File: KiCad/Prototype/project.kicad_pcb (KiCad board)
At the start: 2 copper layers, 68.6 x 53.3 mm, 40 parts, among them J3 Barrel_Jack, Q1 PMOS, SW1 RESET, U1 LP2985-3.3, U2 LMV358, U3 NCP1117-1.5, U4 ATMEGA32U4-AU, X1 USB_OTG, Y1 16 Mhz

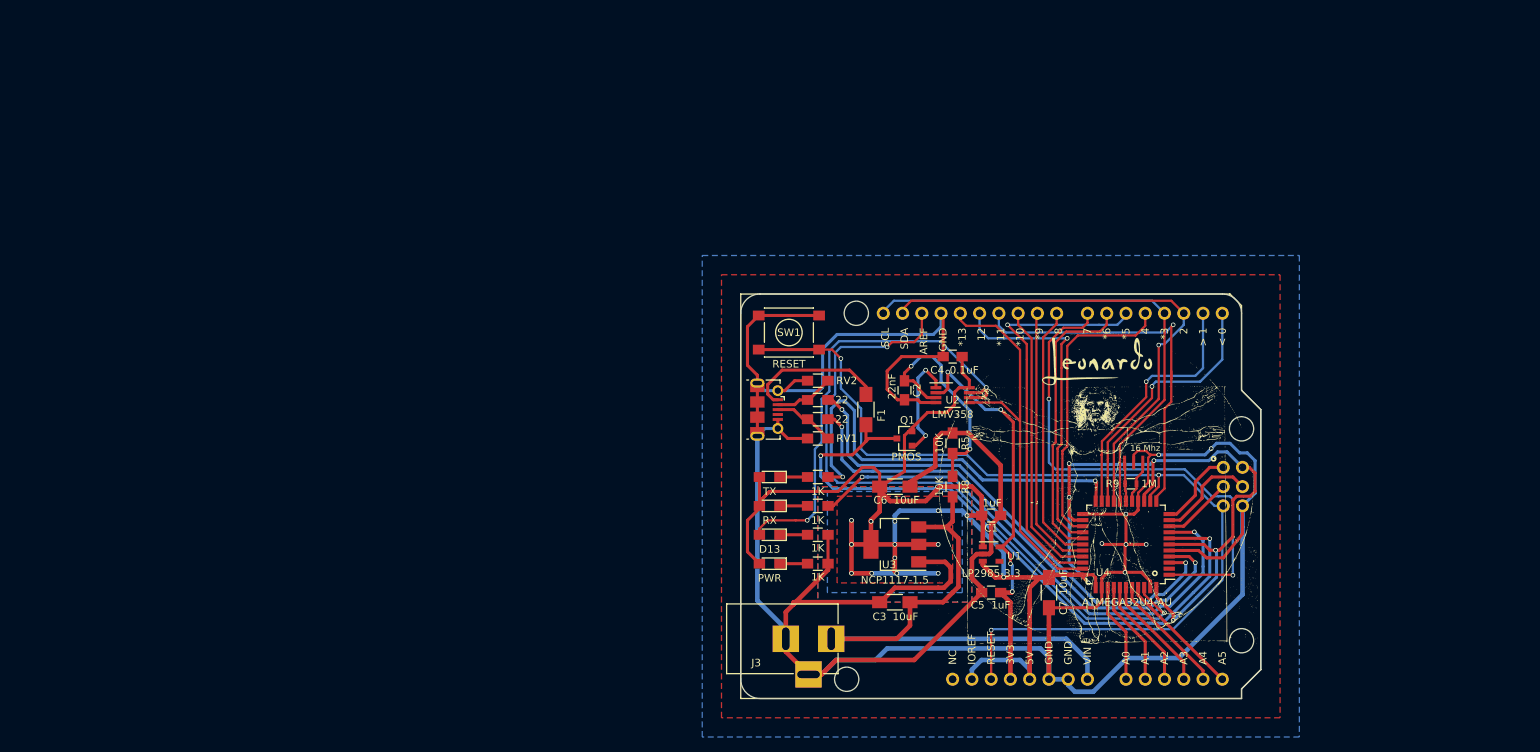
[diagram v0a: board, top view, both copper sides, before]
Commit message: more work on schematic, started layout
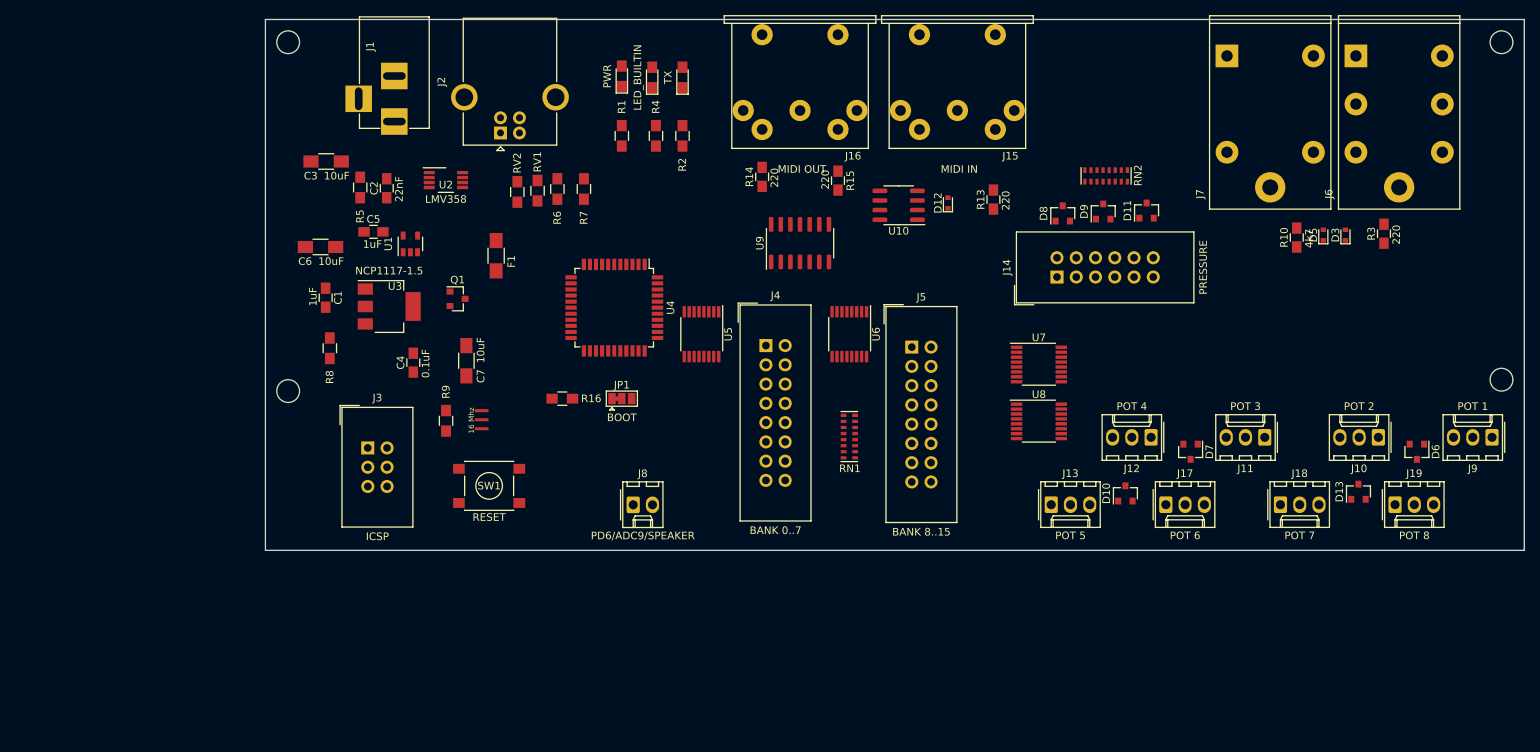
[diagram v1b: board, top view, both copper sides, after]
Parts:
- removed G***: LOGO, footprints:Leo_Front
- removed G***: LOGO, footprints:Leo_back
- removed G*** (x2): LOGO, footprints:graphic_SDA
- removed REF***: KiCad-Logo2_8mm_SilkScreen, Symbols:KiCad-Logo2_8mm_SilkScreen
- removed REF***: OSHW-Logo_5.7x6mm_SilkScreen, Symbols:OSHW-Logo_5.7x6mm_SilkScreen
- removed VAL: MadeInOregonRev25, footprints:MadeInOregonRev25
- removed X1: USB_OTG, footprints:USB_Micro-B_Molex-105017-0001
- removed XA1: Arduino_Leonardo_Shield, footprints:Arduino_Leonardo_Shield
- added D10: BAV70, footprints:SOT-23, F.Cu at (157.4, 102.5)
- added D11: BAV70, footprints:SOT-23, F.Cu at (160.2, 65.2)
- added D12: 1N914WT, footprints:D_SOD-523, F.Cu at (134.0, 64.2)
- added D13: BAV70, footprints:SOT-23, F.Cu at (188.1, 102.3)
- added D5: 1N914WT, footprints:D_SOD-523, F.Cu at (183.5, 68.4)
- added D6: BAV70, footprints:SOT-23, F.Cu at (195.8, 97.0)
- added D7: BAV70, footprints:SOT-23, F.Cu at (166.0, 97.0)
- added D8: BAV70, footprints:SOT-23, F.Cu at (149.1, 65.6)
- added D9: BAV70, footprints:SOT-23, F.Cu at (154.5, 65.3)
- added J1: Barrel_Jack, footprints:BARREL_JACK, F.Cu at (61.0, 53.5)
- added J10: POT 2, footprints:Molex_KK-254_AE-6410-03A_1x03_P2.54mm_Vertical, F.Cu at (190.8, 95.1)
- added J11: POT 3, footprints:Molex_KK-254_AE-6410-03A_1x03_P2.54mm_Vertical, F.Cu at (175.8, 95.1)
- added J12: POT 4, footprints:Molex_KK-254_AE-6410-03A_1x03_P2.54mm_Vertical, F.Cu at (160.8, 95.1)
- added J13: POT 5, footprints:Molex_KK-254_AE-6410-03A_1x03_P2.54mm_Vertical, F.Cu at (147.6, 104.0)
- added J14: PRESSURE, footprints:IDC-Header_2x06_P2.54mm_Vertical, F.Cu at (148.4, 74.0)
- added J15: MIDI IN, footprints:DIN_5_180Deg_PSG03463, F.Cu at (135.2, 52.0)
- added J16: MIDI OUT, footprints:DIN_5_180Deg_PSG03463, F.Cu at (114.5, 52.0)
- added J17: POT 6, footprints:Molex_KK-254_AE-6410-03A_1x03_P2.54mm_Vertical, F.Cu at (162.7, 104.0)
- added J18: POT 7, footprints:Molex_KK-254_AE-6410-03A_1x03_P2.54mm_Vertical, F.Cu at (177.8, 104.0)
- added J19: POT 8, footprints:Molex_KK-254_AE-6410-03A_1x03_P2.54mm_Vertical, F.Cu at (193.0, 104.0)
- added J2: USB_B, footprints:USB_B_OST_USB-B1HSxx_Horizontal, F.Cu at (75.0, 55.0)
- added J4: BANK 0..7, footprints:IDC-Header_2x08_P2.54mm_Vertical, F.Cu at (110.0, 83.0)
- added J5: BANK 8..15, footprints:IDC-Header_2x08_P2.54mm_Vertical, F.Cu at (129.2, 83.2)
- added J6: EXPRESSION, footprints:Jack_6.35mm_Amphenol_ACJS-MHDR, F.Cu at (193.5, 57.5)
- added J7: SUSTAIN, footprints:Jack_6.35mm_Amphenol_ACJM-MHDR, F.Cu at (176.5, 57.5)
- added J8: PD6/ADC9/SPEAKER, footprints:Molex_KK-254_AE-6410-02A_1x02_P2.54mm_Vertical, F.Cu at (92.5, 104.0)
- added J9: POT 1, footprints:Molex_KK-254_AE-6410-03A_1x03_P2.54mm_Vertical, F.Cu at (205.7, 95.1)
- added JP1: BOOT, footprints:SolderJumper-3_P1.3mm_Bridged12_Pad1.0x1.5mm, F.Cu at (91.0, 90.0)
- added R10: 4k7, footprints:C_0805_HandSoldering, F.Cu at (180.0, 68.8)
- added R13: 220, footprints:C_0805_HandSoldering, F.Cu at (140.0, 63.8)
- added R14: 220, footprints:C_0805_HandSoldering, F.Cu at (109.5, 60.8)
- added R15: 220, footprints:C_0805_HandSoldering, F.Cu at (119.5, 61.2)
- added R16: 1K, footprints:R_0805_HandSoldering, F.Cu at (83.2, 90.0)
- added RN1: 4k7, footprints:R_Cat16-8, F.Cu at (121.0, 95.0)
- added RN2: 10k/4k7, footprints:R_Cat16-8, F.Cu at (154.9, 60.6)
- added U10: HCPL-0600, footprints:SOIC-8_3.9x4.9mm_P1.27mm, F.Cu at (127.5, 64.5)
- added U5: 74LS138, footprints:TSSOP-16_4.4x5mm_P0.65mm, F.Cu at (101.5, 81.5)
- added U6: 74LS138, footprints:TSSOP-16_4.4x5mm_P0.65mm, F.Cu at (121.0, 81.5)
- added U7: 74LS238, footprints:TSSOP-16_4.4x5mm_P0.65mm, F.Cu at (146.0, 85.5)
- added U8: 74LS238, footprints:TSSOP-16_4.4x5mm_P0.65mm, F.Cu at (146.0, 93.0)
- added U9: 74HC04, footprints:SOIC-14_3.9x8.7mm_P1.27mm, F.Cu at (114.5, 69.5)
- C1, C2, C4, C5: footprint Capacitors_SMD:C_0805_HandSoldering -> footprints:C_0805_HandSoldering
- C3, C6: footprint Capacitors_SMD:C_1206_HandSoldering -> footprints:C_1206_HandSoldering
- D1, D2: footprint LEDs:LED_0805_HandSoldering -> footprints:LED_0805_HandSoldering
- D3: value RX -> 1N914WT; footprint LEDs:LED_0805_HandSoldering -> footprints:D_SOD-523
- D4: value D13 -> LED_BUILTIN; footprint LEDs:LED_0805_HandSoldering -> footprints:LED_0805_HandSoldering
- F1: footprint Resistors_SMD:R_1206_HandSoldering -> footprints:R_1206_HandSoldering
- J3: value Barrel_Jack -> ICSP; footprint Connectors:BARREL_JACK -> footprints:IDC-Header_2x03_P2.54mm_Vertical
- Q1: footprint TO_SOT_Packages_SMD:SOT-23 -> footprints:SOT-23
- R1, R2, R4, R5, R6, R7, R8, RV1, RV2: footprint Resistors_SMD:R_0805_HandSoldering -> footprints:R_0805_HandSoldering
- R3: value 1K -> 220; footprint Resistors_SMD:R_0805_HandSoldering -> footprints:C_0805_HandSoldering
- R9: footprint Resistors_SMD:R_0603 -> footprints:R_0805_HandSoldering
- SW1: footprint Buttons_Switches_SMD:SW_SPST_PTS645 -> footprints:SW_SPST_PTS645
- U1: footprint TO_SOT_Packages_SMD:SOT-23-5 -> footprints:SOT-23-5
- U2: footprint Housings_SSOP:VSSOP-8_3.0x3.0mm_Pitch0.65mm -> footprints:VSSOP-8_3.0x3.0mm_Pitch0.65mm
- U3: footprint TO_SOT_Packages_SMD:SOT-223-3_TabPin2 -> footprints:SOT-223-3_TabPin2
- moved C3 94.9 mm to (52.0, 58.7)
- moved C5 94.3 mm to (58.2, 68.0)
- moved C1 92.3 mm to (51.9, 76.7), turned to 90 degrees
- moved R9 90.7 mm to (67.8, 92.9), turned to 270 degrees
- moved U1 86.8 mm to (63.1, 69.6), turned to 90 degrees
- moved Y1 86.2 mm to (72.5, 92.8), turned to 90 degrees
- moved R5 85.1 mm to (56.5, 62.1), turned to 90 degrees
- moved R8 84.1 mm to (52.5, 83.3), turned to 90 degrees
- moved D3 83.9 mm to (186.4, 68.4), turned to 90 degrees
- moved R3 82.8 mm to (191.5, 68.2), turned to 270 degrees
- moved C7 82.7 mm to (70.5, 85.0)
- moved C6 82.1 mm to (51.3, 70.0), turned to 180 degrees
- moved U4 74.4 mm to (90.0, 78.0), turned to 270 degrees
- moved U3 73.7 mm to (60.3, 77.9), turned to 0 degrees
- moved C2 73.3 mm to (60.0, 62.2)
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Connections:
- C3 pad 1: /VIN -> +12V
- D3 pad 1: Net-(D3-Pad1) -> /ADC10
- D3 pad 2: +5V -> Net-(D3-Pad2)
- J3 pad 1: /VIN -> /PB3
- J3 pad 2: GND -> +5V
- J3 pad 3: GND -> /PB1
- R3 pad 1: /RXLED -> Net-(J6-PadR)
- R3 pad 2: Net-(D3-Pad1) -> /AMUX1
- R8 pad 2: /VIN -> +12V
- U3 pad 3: /VIN -> +12V
- U4 pad 1: /D7 -> /PE6
- U4 pad 10: /MOSI -> /PB2
- U4 pad 11: /MISO -> /PB3
- U4 pad 12: /D11 -> /PB7
- U4 pad 20: /D0 -> /RXD
- U4 pad 21: /D1 -> /TXD
- U4 pad 25: /D4 -> /PD4
- U4 pad 26: /D12 -> /ADC9
- U4 pad 27: /D6 -> /ADC10
- U4 pad 28: /D8 -> /PB4
- U4 pad 29: /D9 -> /PB5
- U4 pad 30: /D10 -> /PB6
- U4 pad 33: +5V -> /~HWB
- U4 pad 36: /A0 -> /PF7
- U4 pad 37: /A1 -> /PF6
- U4 pad 38: /A2 -> /PF5
- U4 pad 39: /A3 -> /PF4
- U4 pad 40: /A4 -> /PF1
- U4 pad 41: /A5 -> /PF0
- U4 pad 8: /RXLED -> /PB0
- U4 pad 9: /SCK -> /PB1
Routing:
- net GND: track 417.4 -> 0.00 mm, vias 7 -> 0
- net +5V: track 291.0 -> 0.00 mm, vias 20 -> 0
- net /~RESET: track 128.7 -> 0.00 mm, vias 3 -> 0
- net /AREF: track 88.9 -> 0.00 mm, vias 2 -> 0
- net VBUS: track 88.4 -> 0.00 mm, vias 2 -> 0
- net /VIN: track 75.4 -> 0.00 mm
- net /RXLED: track 70.2 -> 0.00 mm, vias 2 -> 0
- net /D+: track 68.2 -> 0.00 mm, vias 2 -> 0
- net /D7: track 68.0 -> 0.00 mm, vias 2 -> 0
- net /SDA: track 67.7 -> 0.00 mm, vias 1 -> 0
- net /D-: track 66.5 -> 0.00 mm, vias 2 -> 0
- net /SCL: track 65.8 -> 0.00 mm
- net Net-(D4-Pad2): track 60.9 -> 0.00 mm, vias 2 -> 0
- net /TXLED: track 57.6 -> 0.00 mm, vias 2 -> 0
- net /D5: track 53.7 -> 0.00 mm, vias 1 -> 0
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- removed copper zone on B.Cu, net +5V
- removed copper zone on F.Cu, net +5V
- removed copper zone on B.Cu, net GND
- removed copper zone on F.Cu, net GND
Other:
- board size 68.6 x 53.3 mm -> 166 x 70 mm
- board text removed: "*10"
- board text removed: "*11"
- board text removed: "*13"
- board text removed: "*3"
- board text removed: "*5"
- board text removed: "*6"
- board text removed: "*9"
- board text removed: "12"
- board text removed: "2"
- board text removed: "3V3"
- board text removed: "4"
- board text removed: "5V"
- board text removed: "7"
- board text removed: "8"
- board text removed: "< 0"
- board text removed: "> 1"
- board text removed: "@TheMakerBox"
- board text removed: "A0"
- board text removed: "A1"
- board text removed: "A2"
- board text removed: "A3"
- board text removed: "A4"
- board text removed: "A5"
- board text removed: "AREF"
- board text removed: "GND"
- board text removed: "IOREF"
- board text removed: "NC"
- board text removed: "RESET"
- board text removed: "Rev 0.0 Sep 2018"
- board text removed: "SCL"
- board text removed: "SDA"
- board text removed: "VIN"
- board text removed: "www.MakersBox.us"

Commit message: more routing
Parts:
- RN1, RN2: footprint footprints:R_Cat16-8 -> Package_SO:SOIC-16_3.9x9.9mm_P1.27mm
- U5, U6, U7, U8: footprint footprints:TSSOP-16_4.4x5mm_P0.65mm -> Package_SO:SOIC-16_3.9x9.9mm_P1.27mm
- moved U8 52.8 mm to (196.0, 76.0), turned to 270 degrees
- moved U7 36.3 mm to (181.0, 76.0), turned to 270 degrees
- moved RN1 24.8 mm to (144.5, 103.0), turned to 90 degrees
- moved U6 22.9 mm to (143.5, 85.5), turned to 180 degrees
- moved U5 17.3 mm to (104.5, 98.5), turned to 0 degrees
- moved C6 17.2 mm to (57.5, 86.0), turned to 270 degrees
- moved D10 8.16 mm to (165.5, 103.5)
- moved D13 7.57 mm to (195.6, 103.3)
- moved J13 7.57 mm to (155.1, 105.0)
- moved J17 7.57 mm to (170.2, 105.0)
- moved J18 7.57 mm to (185.3, 105.0)
- moved J19 7.57 mm to (200.5, 105.0)
- moved R16 7.23 mm to (85.0, 97.0), turned to 0 degrees
- moved J8 7.02 mm to (85.5, 103.5)
- moved J3 6.95 mm to (54.0, 102.5), turned to 90 degrees
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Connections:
- RN1 pad 1: /PB0 -> +5V
- RN1 pad 10: +5V -> /PB6
- RN1 pad 11: +5V -> /PB5
- RN1 pad 12: +5V -> /PB4
- RN1 pad 13: +5V -> /PB3
- RN1 pad 14: +5V -> /PB2
- RN1 pad 15: +5V -> /PB1
- RN1 pad 16: +5V -> /PB0
- RN1 pad 2: /PB1 -> +5V
- RN1 pad 3: /PB2 -> +5V
- RN1 pad 4: /PB3 -> +5V
- RN1 pad 5: /PB4 -> +5V
- RN1 pad 6: /PB5 -> +5V
- RN1 pad 7: /PB6 -> +5V
- RN1 pad 8: /PB7 -> +5V
- RN1 pad 9: +5V -> /PB7
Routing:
- net /PF4: track 0.00 -> 140.6 mm, vias 0 -> 4
- net /PF5: track 0.00 -> 139.7 mm, vias 0 -> 4
- net /PF6: track 0.00 -> 137.9 mm, vias 0 -> 4
- net /PF7: track 0.00 -> 132.7 mm, vias 0 -> 4
- net /PB0: track 0.00 -> 95.6 mm, vias 0 -> 1
- net /PB1: track 0.00 -> 92.1 mm, vias 0 -> 2
- net /PB2: track 0.00 -> 88.5 mm, vias 0 -> 2
- net /PB3: track 0.00 -> 84.2 mm, vias 0 -> 2
- net GND: track 0.00 -> 82.9 mm
- net /PB7: track 0.00 -> 78.7 mm, vias 0 -> 2
- net /PB4: track 0.00 -> 67.2 mm, vias 0 -> 2
- net /PB5: track 0.00 -> 67.0 mm, vias 0 -> 2
- net /PB6: track 0.00 -> 67.0 mm, vias 0 -> 2
- net /~RESET: track 0.00 -> 51.9 mm
- net /AMUX2: track 0.00 -> 38.2 mm
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
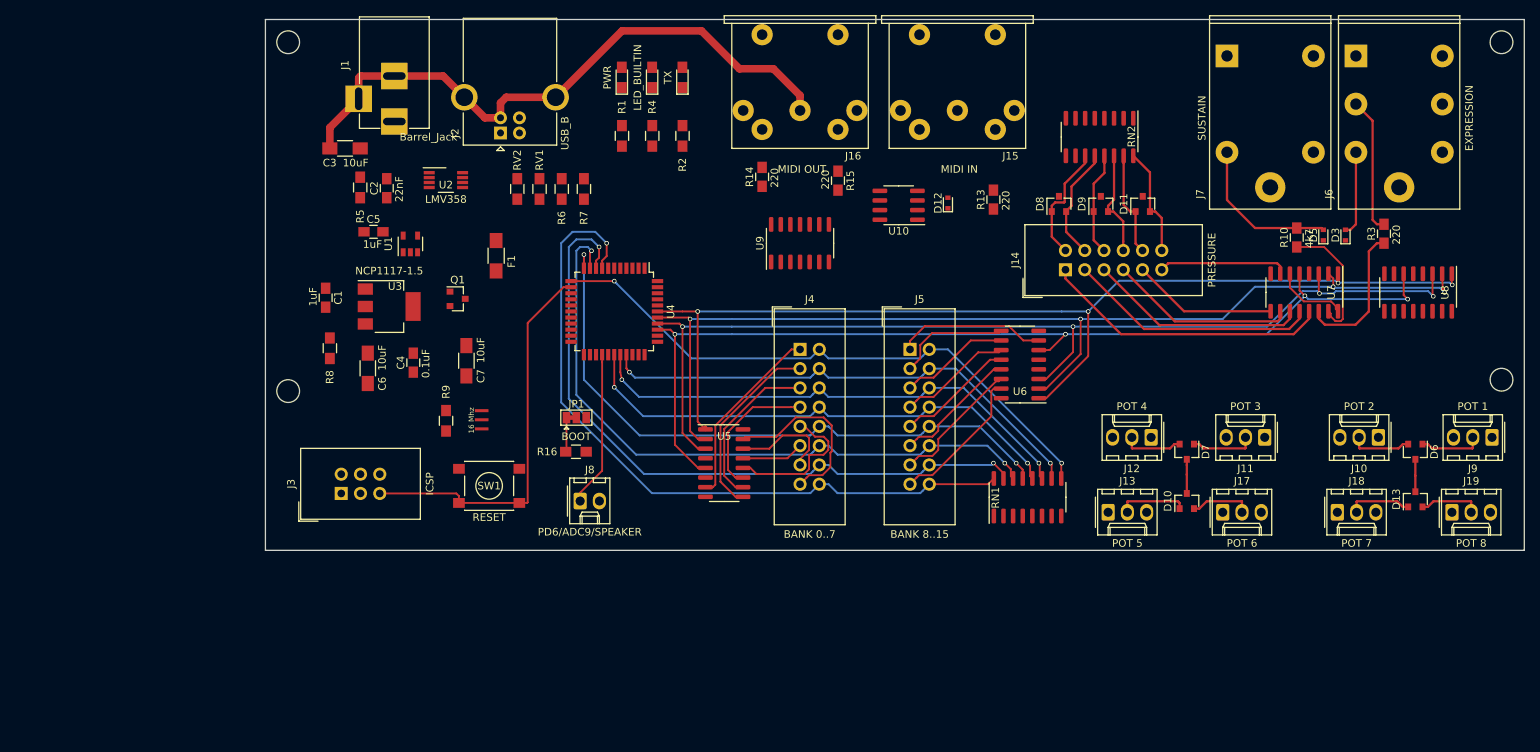
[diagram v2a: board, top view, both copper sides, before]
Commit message: Readying schematic and routing for prototype production
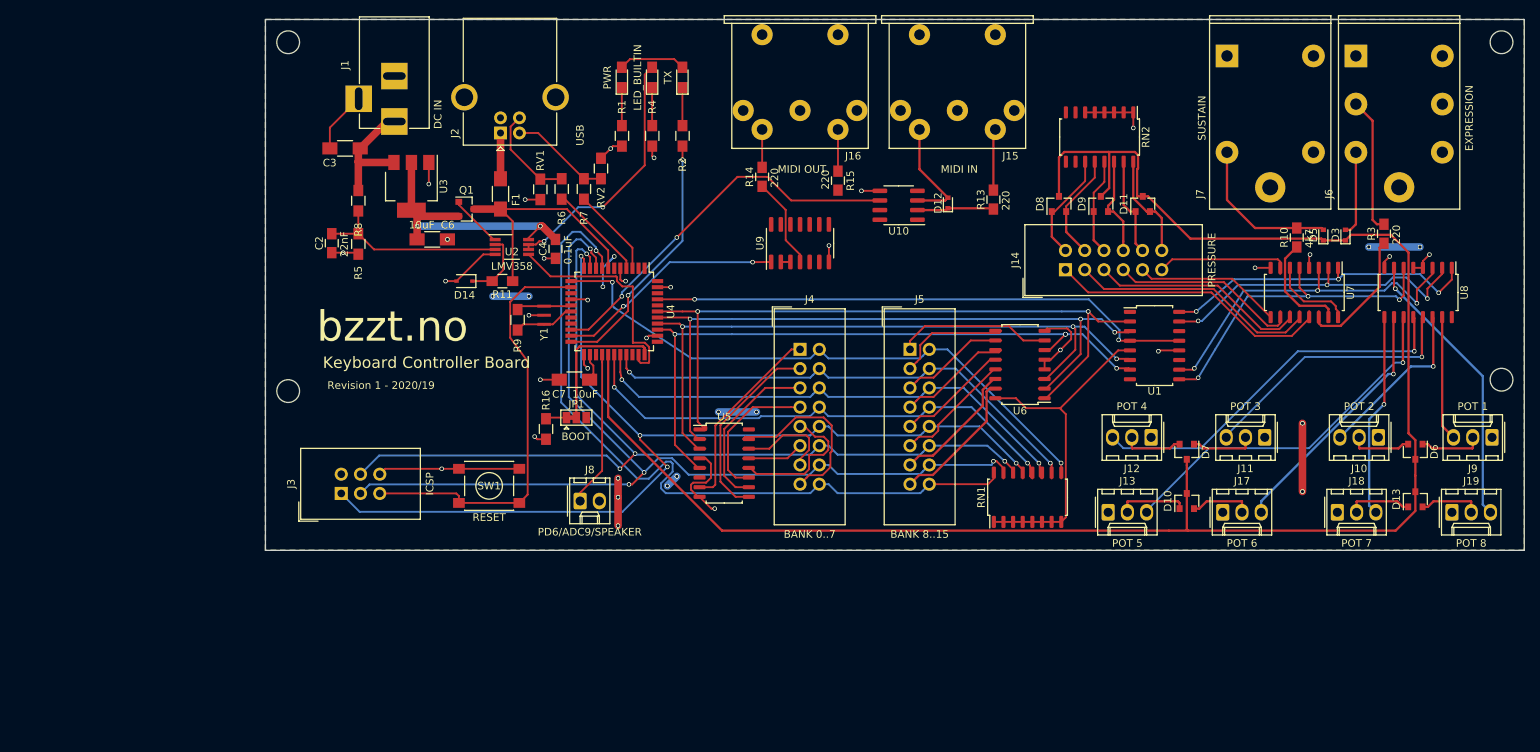
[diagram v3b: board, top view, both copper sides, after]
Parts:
- removed C1, C5: 1uF, footprints:C_0805_HandSoldering
- added D14: BZX384-xxx, Diode_SMD:D_SOD-323, F.Cu at (70.2, 74.5)
- added R11: 10K, footprints:R_0805_HandSoldering, F.Cu at (75.2, 74.5)
- J1: value Barrel_Jack -> DC IN
- J2: value USB_B -> USB
- RN1, RN2, U5, U6, U7, U8: footprint Package_SO:SOIC-16_3.9x9.9mm_P1.27mm -> footprints:SOIC-16_4.55x10.3mm_P1.27mm
- U1: value LP2985-3.3 -> 74LS75; footprint footprints:SOT-23-5 -> footprints:SOIC-16_4.55x10.3mm_P1.27mm
- moved U1 99.0 mm to (161.2, 83.0), turned to 0 degrees
- moved C4 24.0 mm to (82.2, 70.2)
- moved R8 19.8 mm to (56.2, 63.9)
- moved C6 19.0 mm to (66.0, 69.0), turned to 0 degrees
- moved R9 16.3 mm to (77.2, 79.6)
- moved U3 16.1 mm to (63.2, 62.0), turned to 270 degrees
- moved Y1 16.1 mm to (80.8, 79.0)
- moved C7 14.5 mm to (84.8, 87.5), turned to 180 degrees
- moved U2 12.4 mm to (76.5, 70.0)
- moved Q1 11.9 mm to (70.5, 65.0)
- moved RV2 11.4 mm to (88.2, 59.6), turned to 90 degrees
- moved C2 10.3 mm to (52.8, 69.5)
- moved F1 8.17 mm to (75.0, 63.0)
- moved R5 7.45 mm to (56.2, 69.6)
- moved R16 4.96 mm to (81.0, 94.0), turned to 270 degrees
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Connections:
- U1 pad 1: +5V -> Net-(U1-Pad1)
- U1 pad 2: GND -> /PF4
- U1 pad 3: +5V -> /PF5
- U1 pad 4: Net-(U1-Pad4) -> /PF0
- U1 pad 5: +3V3 -> +5V
- U7 pad 1: /PF4 -> /AEN0
- U7 pad 2: /PF5 -> /AEN1
- U7 pad 3: /PF6 -> /AEN2
- U7 pad 5: /PF7 -> /AEN3
- U8 pad 1: /PF4 -> /AEN0
- U8 pad 2: /PF5 -> /AEN1
- U8 pad 3: /PF6 -> /AEN2
- U8 pad 6: /PF7 -> /AEN3
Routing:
- net /ADC10: track 8.77 -> 233.2 mm
- net +5V: track 9.69 -> 130.9 mm, vias 0 -> 12
- net /PF0: track 0.00 -> 72.0 mm, vias 0 -> 2
- net /PB3: track 84.2 -> 136.2 mm, vias 2 -> 4
- net /RXD: track 0.00 -> 50.7 mm, vias 0 -> 2
- net /AMUX11: track 0.00 -> 50.2 mm, vias 0 -> 1
- net /AMUX12: track 0.00 -> 48.1 mm, vias 0 -> 1
- net /PF5: track 139.7 -> 92.4 mm, vias 4 -> 3
- net /AEN2: track 0.00 -> 47.1 mm, vias 0 -> 3
- net /PF4: track 140.6 -> 93.8 mm, vias 4 -> 2
- net /PF6: track 137.9 -> 91.8 mm, vias 4 -> 3
- net /PF7: track 132.7 -> 87.3 mm
- net GND: track 82.9 -> 128.2 mm, vias 0 -> 32
- net /AEN3: track 0.00 -> 44.0 mm, vias 0 -> 3
- net /AEN1: track 0.00 -> 43.5 mm, vias 0 -> 3
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- added copper zone on F.Cu, net +5V
- added copper zone on B.Cu, net GND
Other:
- board text added: "Keyboard Controller Board"
- board text added: "Revision 1 - 2020/19"
- board text added: "bzzt.no"

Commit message: minor tweaks
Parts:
- removed D5: 1N914WT, footprints:D_SOD-523
- added J20: TTL MIDI, footprints:Molex_KK-254_AE-6410-03A_1x03_P2.54mm_Vertical, F.Cu at (122.6, 72.4)
- added JP2: PULLUP, footprints:SolderJumper-3_P1.3mm_Bridged12_Pad1.0x1.5mm, F.Cu at (150.6, 94.6)
- added JP3: PULLUP, footprints:SolderJumper-3_P1.3mm_Bridged12_Pad1.0x1.5mm, F.Cu at (163.6, 45.2)
- D14: value BZX384-xxx -> ZMM3V3; footprint Diode_SMD:D_SOD-323 -> Diode_SMD:D_MiniMELF
- D3: value 1N914WT -> BAV70; footprint footprints:D_SOD-523 -> footprints:SOT-23
- F1: value Polyfuse -> 0
- J1: value DC IN -> Barrel_Jack
- J2: value USB -> USB_B
- JP1: footprint footprints:SolderJumper-3_P1.3mm_Bridged12_Pad1.0x1.5mm -> Jumper:SolderJumper-2_P1.3mm_Open_Pad1.0x1.5mm
- Q1: value PMOS -> PMV48XP,215
- R16: value 1K -> 10K
- RV1, RV2: value Varistor -> P6SMB6.8CA; footprint footprints:R_0805_HandSoldering -> Diode_SMD:D_SMB
- U3: value NCP1117-1.5 -> AMS1117-5.0
- U5, U6: value 74LS138 -> 74HC138
- U7, U8: value 74LS238 -> 74HC238
- moved RV2 3.56 mm to (87.6, 56.1)
- moved JP1 2.30 mm to (85.0, 94.8), turned to 270 degrees
- moved D3 1.88 mm to (185.0, 67.2)
- moved R6 0.73 mm to (83.8, 62.4)
- moved R16 0.40 mm to (80.6, 94.0)
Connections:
- net +3V3 renamed Net-(D14-Pad1)
- D3 pad 1: /ADC10 -> Net-(D3-Pad1)
- J7 pad T: Net-(D5-Pad2) -> Net-(D3-Pad1)
- JP1 pad 1: Net-(JP1-Pad1) -> /~HWB
- JP1 pad 2: /~HWB -> +5V
- R10 pad 1: Net-(D5-Pad2) -> Net-(D3-Pad1)
- R16 pad 1: Net-(JP1-Pad1) -> GND
- R16 pad 2: GND -> /~HWB
- RN1 pad 1: +5V -> Net-(JP2-Pad2)
- RN1 pad 2: +5V -> Net-(JP2-Pad2)
- RN1 pad 3: +5V -> Net-(JP2-Pad2)
- RN1 pad 4: +5V -> Net-(JP2-Pad2)
- RN1 pad 5: +5V -> Net-(JP2-Pad2)
- RN1 pad 6: +5V -> Net-(JP2-Pad2)
- RN1 pad 7: +5V -> Net-(JP2-Pad2)
- RN1 pad 8: +5V -> Net-(JP2-Pad2)
- RN2 pad 1: GND -> Net-(JP3-Pad2)
- RN2 pad 2: GND -> Net-(JP3-Pad2)
- RN2 pad 3: GND -> Net-(JP3-Pad2)
- RN2 pad 4: GND -> Net-(JP3-Pad2)
- RN2 pad 5: GND -> Net-(JP3-Pad2)
- RN2 pad 6: GND -> Net-(JP3-Pad2)
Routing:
- net Net-(JP2-Pad2): track 0.00 -> 21.6 mm
- net Net-(D3-Pad1): track 0.00 -> 21.4 mm
- net Net-(D5-Pad2): track 20.6 -> 0.00 mm
- net /TXD: track 31.2 -> 47.6 mm
- net Net-(JP3-Pad2): track 0.00 -> 15.5 mm
- net GND: track 128.2 -> 143.0 mm, vias 32 -> 30
- net /RXD: track 50.7 -> 60.7 mm
- net +5V: track 130.9 -> 124.0 mm, vias 12 -> 14
- net /~HWB: track 19.1 -> 25.6 mm
- net /ADC10: track 233.2 -> 236.1 mm
- net Net-(J2-Pad3): track 13.0 -> 10.2 mm
- net Net-(JP1-Pad1): track 2.76 -> 0.00 mm
- net VBUS: track 32.5 -> 30.1 mm
- net Net-(J2-Pad2): track 13.2 -> 14.4 mm
- net /D+: track 12.9 -> 12.3 mm
